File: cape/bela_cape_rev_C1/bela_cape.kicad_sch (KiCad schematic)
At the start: 27 parts, among them J1 Conn_01x02, J10 Conn_01x04, J11 Conn_01x02, J2 Conn_01x04, J3 Conn_01x03, J4 Conn_01x03, J5 Conn_01x02, J6 Conn_01x02, J7 Conn_01x10, J8 Conn_01x10, J9 Conn_01x04, P1 BeagleBone_Black_Header

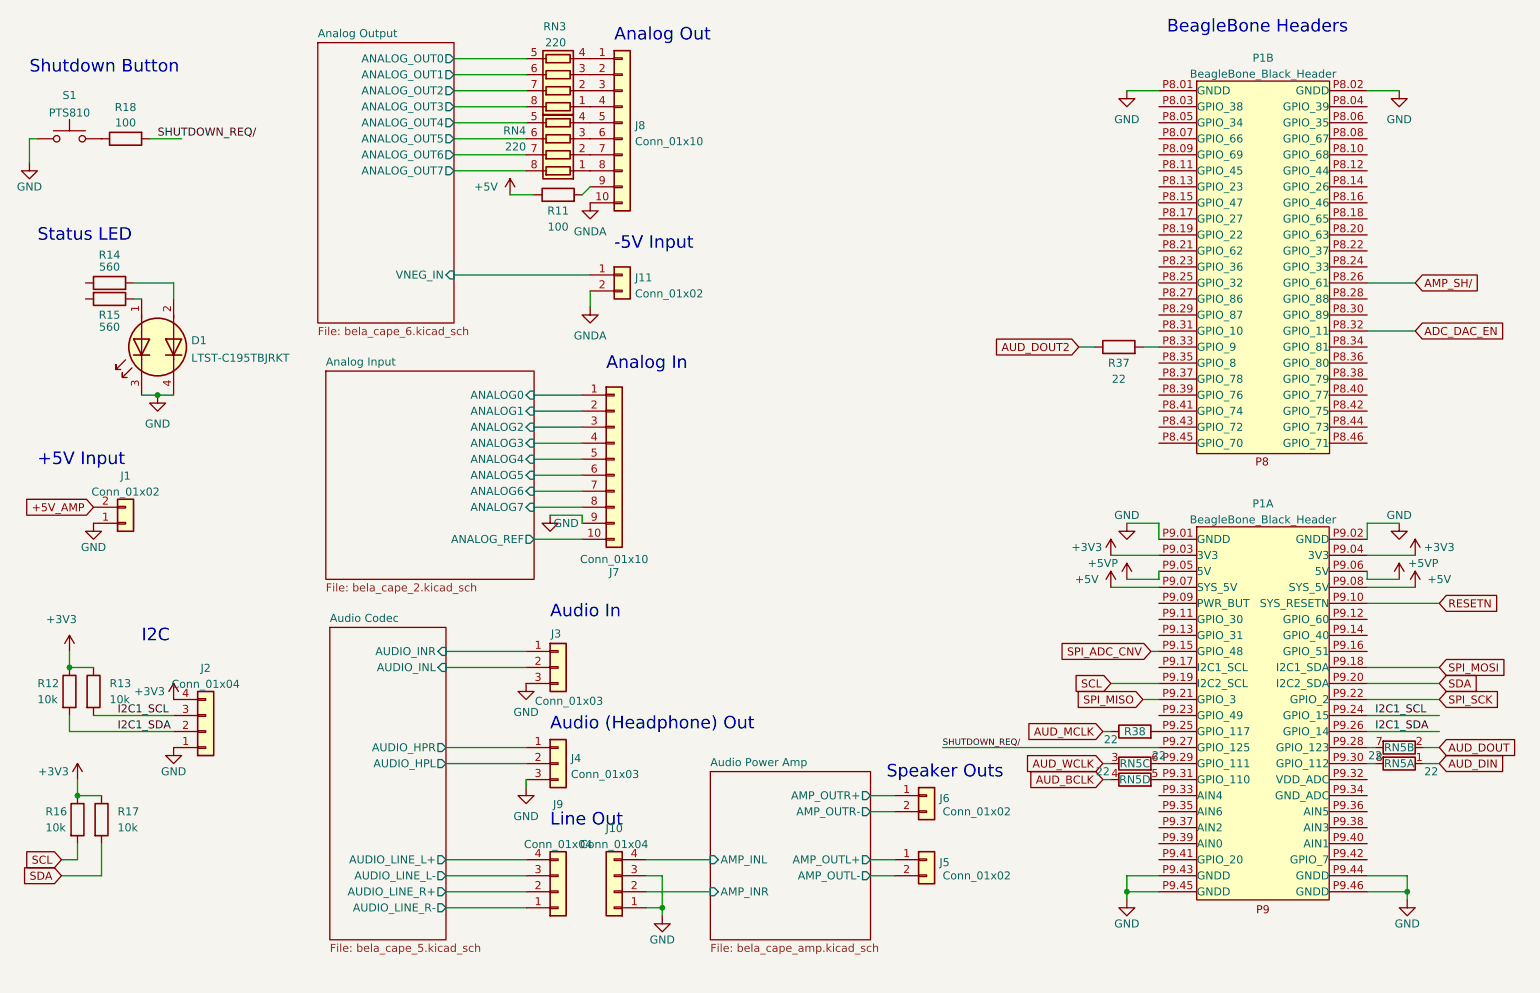
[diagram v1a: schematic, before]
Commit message: More C1 cape routing
(cherry picked from commit db7d999e21b46c22925661ce0002776775f31ffd)
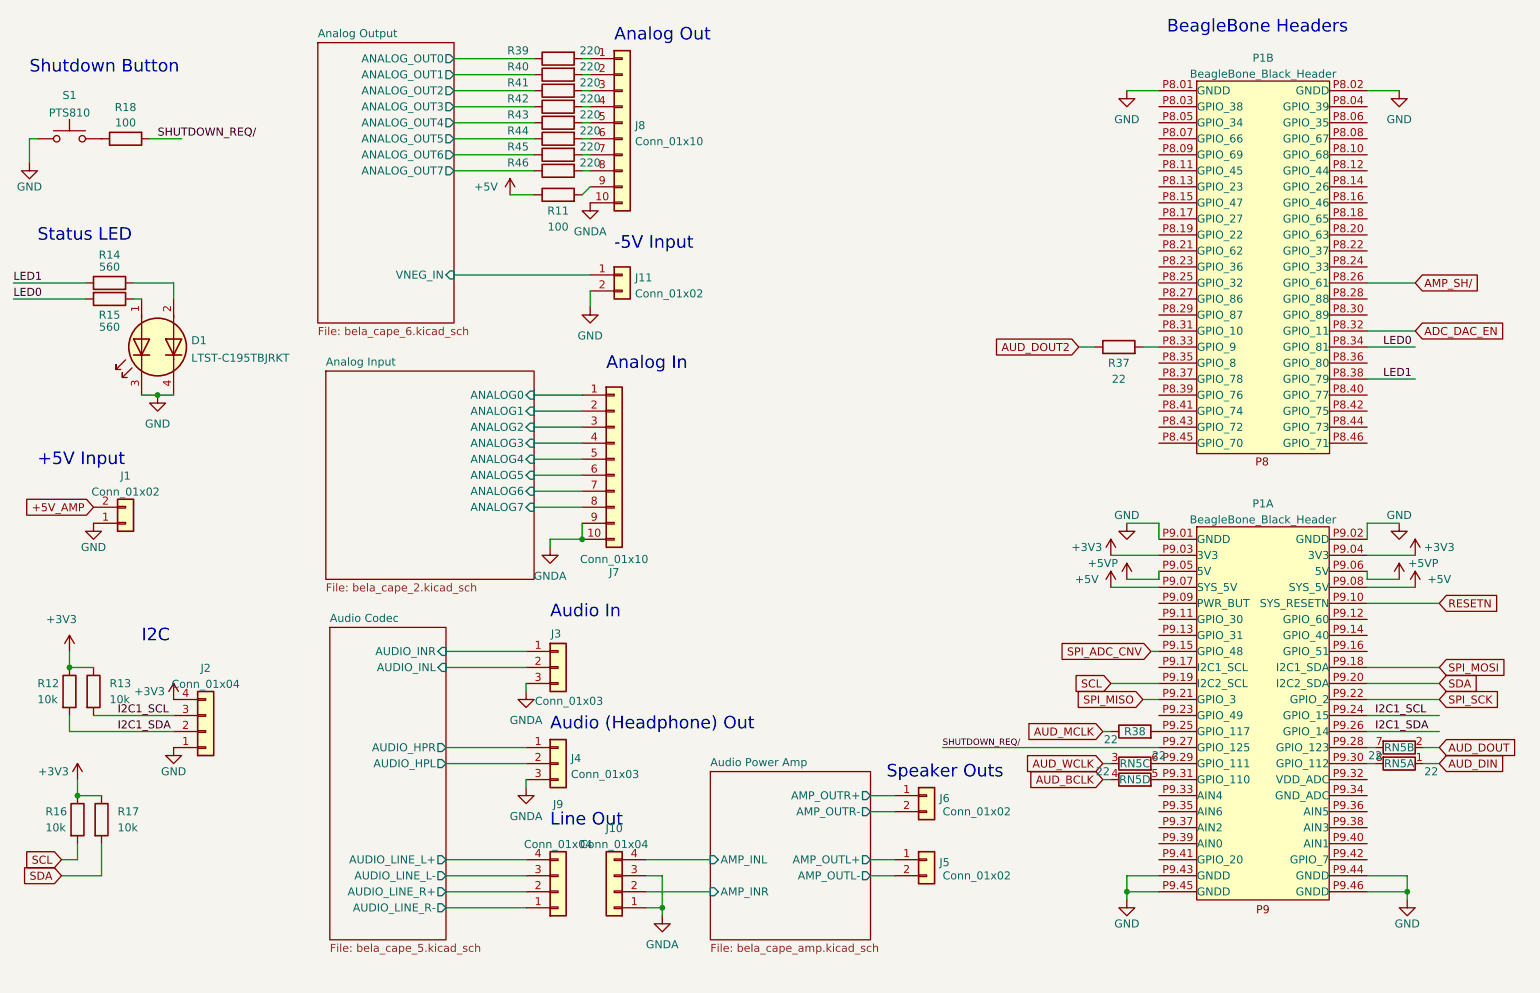
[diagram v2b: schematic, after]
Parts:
- removed RN3, RN4: 220, Resistor_SMD:R_Array_Convex_4x0603, symbol Device:R_Pack04
- added R39, R40, R41, R42, R43, R44, R45, R46: 220, Resistor_SMD:R_0603_1608Metric, symbol Device:R
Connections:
- net Analog Input/ANALOG_REF is gone; now on net GNDA: J7.10 (Pin_10)
- net Analog Output/ANALOG_OUT0: now also R39.1
- net Analog Output/ANALOG_OUT1: now also R40.1
- net Analog Output/ANALOG_OUT2: now also R41.1
- net Analog Output/ANALOG_OUT3: now also R42.1
- net Analog Output/ANALOG_OUT4: now also R43.1
- net Analog Output/ANALOG_OUT5: now also R44.1
- net Analog Output/ANALOG_OUT6: now also R45.1
- net Analog Output/ANALOG_OUT7: now also R46.1
- net GND: now also J11.2 (Pin_2); no longer J10.1 (Pin_1), J10.3 (Pin_3), J3.3 (Pin_3), J4.3 (Pin_3), J7.9 (Pin_9)
- net GNDA: now also J10.1 (Pin_1), J10.3 (Pin_3), J3.3 (Pin_3), J4.3 (Pin_3), J7.9 (Pin_9); no longer J11.2 (Pin_2)
- net at J8.8 (Pin_8): now also R46.2
- net at J8.7 (Pin_7): now also R45.2
- net at J8.6 (Pin_6): now also R44.2
- net at J8.5 (Pin_5): now also R43.2
- net LED0: now reaches R15.2
- net LED0: now also P1.P8.34 (GPIO_81)
- net LED1: now reaches P1.P8.38 (GPIO_79)
- net LED1: now also R14.1
- net at J8.4 (Pin_4): now also R42.2
- net at J8.3 (Pin_3): now also R41.2
- net at J8.2 (Pin_2): now also R40.2
- net at J8.1 (Pin_1): now also R39.2
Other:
- sheet Analog Input ports: added none; removed ANALOG_REF

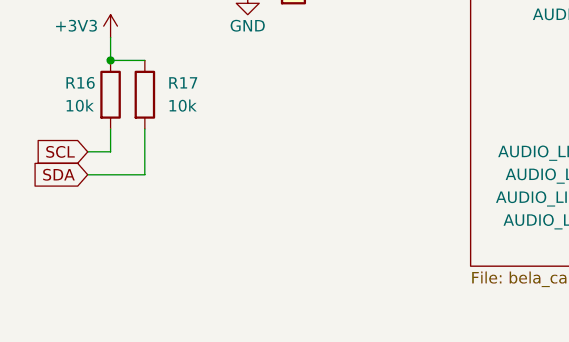
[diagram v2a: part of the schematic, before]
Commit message: Further routing on C1 cape
(cherry picked from commit 232a25b01e013bf194cdc3a343766aa7b43870aa)
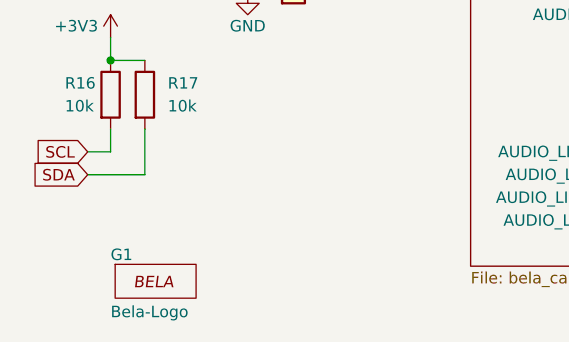
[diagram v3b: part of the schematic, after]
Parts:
- added G1: Bela-Logo, Bela:Bela-Logo_30mm_Silkscreen, symbol Bela:Bela-Logo
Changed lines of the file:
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@@
   (symbol (lib_id "power:GNDA") (at 106.68 102.87 0) (unit 1)
     (in_bom yes) (on_board yes) (fields_autoplaced)
-    (property "Reference" "#PWR?" (id 0) (at 106.68 109.22 0)
+    (property "Reference" "#PWR0125" (id 0) (at 106.68 109.22 0)
       (effects (font (size 1.27 1.27)) hide)
     )
@@
     (pin "1")
   )
+  (symbol (lib_id "Bela:Bela-Logo") (at 36.83 172.72 0) (unit 1)
+    (in_bom no) (on_board yes)
+    (property "Reference" "G1" (id 0) (at 31.75 163.83 0)
+      (effects (font (size 1.27 1.27)) (justify left))
+    )
+    (property "Value" "Bela-Logo" (id 1) (at 31.75 170.18 0)
+      (effects (font (size 1.27 1.27)) (justify left))
+    )
+    (property "Footprint" "Bela:Bela-Logo_30mm_Silkscreen" (id 2) (at 36.83 172.72 0)
+      (effects (font (size 1.27 1.27)) hide)
+    )
+    (property "Datasheet" "" (id 3) (at 36.83 172.72 0)
+      (effects (font (size 1.27 1.27)) hide)
+    )
+  )
   (symbol (lib_id "Device:R") (at 107.95 40.64 90) (mirror x) (unit 1)
     (in_bom yes) (on_board yes)
@@
       (reference "#PWR027") (unit 1) (value "GND") (footprint "")
     )
-    (path "/9e34013b-8051-4e0b-88b6-b650bff5b520/40dc4dd6-803e-4da8-9a03-c94c4fe33765"
-      (reference "#PWR028") (unit 1) (value "+5V") (footprint "")
-    )
     (path "/9e34013b-8051-4e0b-88b6-b650bff5b520/800e6cb7-da14-417f-b31e-4bfa5763b429"
       (reference "#PWR029") (unit 1) (value "GND") (footprint "")
@@
       (reference "#PWR035") (unit 1) (value "GNDA") (footprint "")
     )
-    (path "/c174e798-0d4a-4ee5-a279-22c30e2ae073/4f40af54-d1f9-4e63-9ed7-0c1cc9a787b3"
-      (reference "#PWR042") (unit 1) (value "+3V3") (footprint "")
-    )
     (path "/c174e798-0d4a-4ee5-a279-22c30e2ae073/7d8f34a4-6de6-4535-896b-92ece08d83cf"
       (reference "#PWR043") (unit 1) (value "GNDA") (footprint "")
     )
-    (path "/c174e798-0d4a-4ee5-a279-22c30e2ae073/57271557-8206-4f46-ad35-fc278dec1a36"
-      (reference "#PWR044") (unit 1) (value "+3V3") (footprint "")
-    )
-    (path "/c174e798-0d4a-4ee5-a279-22c30e2ae073/a2635e4f-4386-4ea3-8471-6230f4547d9b"
-      (reference "#PWR045") (unit 1) (value "+3V3") (footprint "")
-    )
     (path "/c174e798-0d4a-4ee5-a279-22c30e2ae073/99b6def2-b64c-456e-a08b-d2899efab4d9"
       (reference "#PWR046") (unit 1) (value "GNDA") (footprint "")
@@
       (reference "#PWR050") (unit 1) (value "GNDA") (footprint "")
     )
-    (path "/c174e798-0d4a-4ee5-a279-22c30e2ae073/c4832e50-a896-4931-9a56-34ef69b486d7"
-      (reference "#PWR051") (unit 1) (value "+3V3") (footprint "")
-    )
-    (path "/c174e798-0d4a-4ee5-a279-22c30e2ae073/339079dd-7e2b-4913-a3d9-1c12f21caf6d"
-      (reference "#PWR053") (unit 1) (value "+3V3") (footprint "")
-    )
     (path "/c174e798-0d4a-4ee5-a279-22c30e2ae073/0fe7d231-05a4-4403-abb8-ecf2f3d64eb2"
       (reference "#PWR054") (unit 1) (value "GNDA") (footprint "")
@@
       (reference "#PWR0124") (unit 1) (value "+3V3") (footprint "")
     )
+    (path "/11483658-07b7-40c4-9227-04f011f4d8dc"
+      (reference "#PWR0125") (unit 1) (value "GNDA") (footprint "")
+    )
+    (path "/ccc90cba-37a2-450c-9fab-b7472fcd4e10/55aafa5a-afd6-402c-808b-c3b09bdda3cc"
+      (reference "#PWR0126") (unit 1) (value "GNDA") (footprint "")
+    )
+    (path "/ccc90cba-37a2-450c-9fab-b7472fcd4e10/e68c39fe-a703-4bee-9202-eb4f3fb840b9"
+      (reference "#PWR0127") (unit 1) (value "GNDA") (footprint "")
+    )
     (path "/ccc90cba-37a2-450c-9fab-b7472fcd4e10/ab3d2859-b070-4137-a246-1110b00c03bf"
       (reference "#PWR0128") (unit 1) (value "GND") (footprint "")
     )
+    (path "/ccc90cba-37a2-450c-9fab-b7472fcd4e10/ed98387a-24f5-4d34-99a5-c4416ebd3917"
+      (reference "#PWR0129") (unit 1) (value "GNDA") (footprint "")
+    )
     (path "/c174e798-0d4a-4ee5-a279-22c30e2ae073/b2758721-3c0e-4941-a062-22e8ce2923aa"
       (reference "#PWR0130") (unit 1) (value "GNDA") (footprint "")
     )
+    (path "/ccc90cba-37a2-450c-9fab-b7472fcd4e10/553bc0ca-d39e-44ff-967b-11d354f2df22"
+      (reference "#PWR0131") (unit 1) (value "GNDA") (footprint "")
+    )
     (path "/c174e798-0d4a-4ee5-a279-22c30e2ae073/dbe0da48-cab3-4cae-93bc-1719de927669"
       (reference "#PWR0132") (unit 1) (value "GND") (footprint "")
@@
       (reference "#PWR0145") (unit 1) (value "GNDA") (footprint "")
     )
+    (path "/ccc90cba-37a2-450c-9fab-b7472fcd4e10/a8c0901b-e42c-4f8f-8c8d-0a18f90dfce3"
+      (reference "#PWR0146") (unit 1) (value "GNDA") (footprint "")
+    )
     (path "/d38e70a7-7ea3-4761-8b86-372920872c36"
       (reference "#PWR0147") (unit 1) (value "GND") (footprint "")
@@
       (reference "#PWR0156") (unit 1) (value "GNDA") (footprint "")
     )
-    (path "/11483658-07b7-40c4-9227-04f011f4d8dc"
-      (reference "#PWR?") (unit 1) (value "GNDA") (footprint "")
-    )
-    (path "/ccc90cba-37a2-450c-9fab-b7472fcd4e10/553bc0ca-d39e-44ff-967b-11d354f2df22"
-      (reference "#PWR?") (unit 1) (value "GNDA") (footprint "")
-    )
-    (path "/ccc90cba-37a2-450c-9fab-b7472fcd4e10/55aafa5a-afd6-402c-808b-c3b09bdda3cc"
-      (reference "#PWR?") (unit 1) (value "GNDA") (footprint "")
-    )
-    (path "/ccc90cba-37a2-450c-9fab-b7472fcd4e10/a8c0901b-e42c-4f8f-8c8d-0a18f90dfce3"
-      (reference "#PWR?") (unit 1) (value "GNDA") (footprint "")
-    )
-    (path "/ccc90cba-37a2-450c-9fab-b7472fcd4e10/e68c39fe-a703-4bee-9202-eb4f3fb840b9"
-      (reference "#PWR?") (unit 1) (value "GNDA") (footprint "")
-    )
-    (path "/ccc90cba-37a2-450c-9fab-b7472fcd4e10/ed98387a-24f5-4d34-99a5-c4416ebd3917"
+    (path "/9e34013b-8051-4e0b-88b6-b650bff5b520/336155f3-725b-4fdb-88c3-38ef43468eed"
+      (reference "#PWR0157") (unit 1) (value "+5VP") (footprint "")
+    )
+    (path "/c174e798-0d4a-4ee5-a279-22c30e2ae073/0957985e-157d-498c-825f-8ecca5e25911"
+      (reference "#PWR0158") (unit 1) (value "+3V3") (footprint "")
+    )
+    (path "/c174e798-0d4a-4ee5-a279-22c30e2ae073/fdd0b81f-0602-4f3d-8c4e-a4ad2e89fc31"
+      (reference "#PWR0159") (unit 1) (value "+3V3") (footprint "")
+    )
+    (path "/c174e798-0d4a-4ee5-a279-22c30e2ae073/3301c3dd-e6a7-413c-aa4b-3c70732c9367"
+      (reference "#PWR0160") (unit 1) (value "+3V3") (footprint "")
+    )
+    (path "/c174e798-0d4a-4ee5-a279-22c30e2ae073/8da74633-6a98-40f2-ab4b-b6e27c3b6b34"
+      (reference "#PWR0161") (unit 1) (value "+3V3") (footprint "")
+    )
+    (path "/c174e798-0d4a-4ee5-a279-22c30e2ae073/76c9b218-46f2-4ee1-bfb4-17d160e6e689"
+      (reference "#PWR0162") (unit 1) (value "+3V3") (footprint "")
+    )
+    (path "/2bd1dbb7-18bf-4e07-b6f1-ffaff520c436/b8672b5b-8694-4112-b948-606619586858"
+      (reference "#PWR0163") (unit 1) (value "GNDA") (footprint "")
+    )
+    (path "/2bd1dbb7-18bf-4e07-b6f1-ffaff520c436/c3957330-a5cd-4893-9391-dc2b65d86c1b"
+      (reference "#PWR0164") (unit 1) (value "GND") (footprint "")
+    )
+    (path "/c174e798-0d4a-4ee5-a279-22c30e2ae073/054bda83-89e7-4fa5-a640-5eefa915414c"
+      (reference "#PWR0165") (unit 1) (value "GNDA") (footprint "")
+    )
+    (path "/c174e798-0d4a-4ee5-a279-22c30e2ae073/c9269e2d-dd2a-454f-aba5-11df90ef9660"
+      (reference "#PWR0166") (unit 1) (value "GND") (footprint "")
+    )
+    (path "/ccc90cba-37a2-450c-9fab-b7472fcd4e10/e0475f41-2cb2-4300-808f-712163d9652a"
+      (reference "#PWR0167") (unit 1) (value "GNDA") (footprint "")
+    )
+    (path "/ccc90cba-37a2-450c-9fab-b7472fcd4e10/d3c7c465-5e5a-4712-a49a-fa72294f762d"
+      (reference "#PWR0168") (unit 1) (value "GND") (footprint "")
+    )
+    (path "/c174e798-0d4a-4ee5-a279-22c30e2ae073/192408a6-4ca2-45dc-b931-ecb620d1338c"
       (reference "#PWR?") (unit 1) (value "GNDA") (footprint "")
     )
@@
       (reference "FB3") (unit 1) (value "MPZ1608S121ATAH0") (footprint "Inductor_SMD:L_0603_1608Metric")
     )
+    (path "/5abaaa3a-7d76-4705-abc2-659d6c295f73"
+      (reference "G1") (unit 1) (value "Bela-Logo") (footprint "Bela:Bela-Logo_30mm_Silkscreen")
+    )
     (path "/2bd1dbb7-18bf-4e07-b6f1-ffaff520c436/261a6a15-e184-4400-a041-3ee93d7fc184"
       (reference "IC1") (unit 1) (value "TLV320AIC3104") (footprint "Package_DFN_QFN:QFN-32-1EP_5x5mm_P0.5mm_EP3.3x3.3mm")
@@
       (reference "JP1") (unit 1) (value "SolderJumper_2_Bridged") (footprint "Jumper:SolderJumper-2_P1.3mm_Bridged_Pad1.0x1.5mm")
     )
+    (path "/2bd1dbb7-18bf-4e07-b6f1-ffaff520c436/899b787e-47b7-452e-ab5a-a0d358f0dd43"
+      (reference "JP2") (unit 1) (value "SolderJumper_2_Bridged") (footprint "Jumper:SolderJumper-2_P1.3mm_Bridged_Pad1.0x1.5mm")
+    )
+    (path "/c174e798-0d4a-4ee5-a279-22c30e2ae073/57f024cb-3826-49a4-bf07-c4f06821fc17"
+      (reference "JP3") (unit 1) (value "SolderJumper_2_Bridged") (footprint "Jumper:SolderJumper-2_P1.3mm_Bridged_Pad1.0x1.5mm")
+    )
+    (path "/ccc90cba-37a2-450c-9fab-b7472fcd4e10/50768e8d-6c06-4585-946d-337ae7200de6"
+      (reference "JP4") (unit 1) (value "SolderJumper_2_Bridged") (footprint "Jumper:SolderJumper-2_P1.3mm_Bridged_Pad1.0x1.5mm")
+    )
     (path "/dd1db79d-77ca-4802-9ac0-4286dd4d6f0d"
